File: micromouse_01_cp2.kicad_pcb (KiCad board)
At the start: 4 copper layers, 52 x 60 mm, 94 parts, among them IC1 MPU-6500, IC2 DRV8835DSSR, IC3 ADS7066IRTER, IC4 PCA9632TK,118, J2 Fan+, J3 Fan-, J4 Battery, J5 Battery, M1 MK06-4.5, M2 MK06-4.5, Q1 SiA910, Q5 SiA519, Q6 SiA519, Q7 SiA519, Q8 SiA519, Q9 SSM6J808R_LXHF, SW1 SSSS810701, U1 MA730, U10 LBR-127HLD, U11 LBR-127HLD, U12 ESP32-S3-MINI-1-N8, U2 MA730, U4 SMT-0440-S-R, U5 WS2812-2020, U7 LXDC55FAAA-203, U8 LBR-127HLD, U9 LBR-127HLD

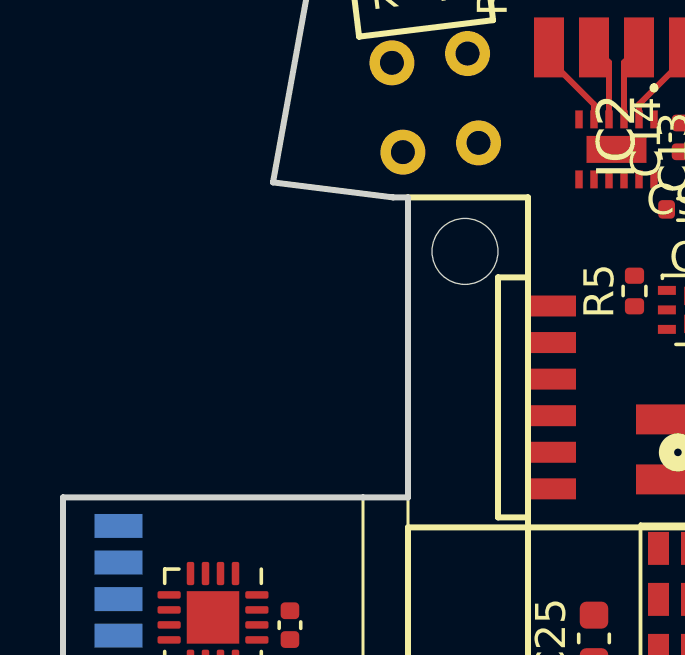
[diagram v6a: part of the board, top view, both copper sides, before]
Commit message: change encoder footprint
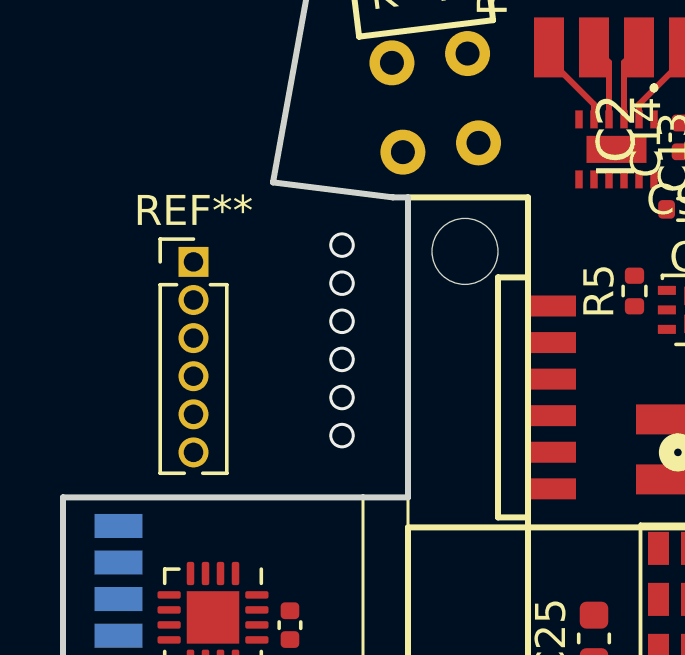
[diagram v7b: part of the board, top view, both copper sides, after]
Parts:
- added REF**: PinHeader_1x06_P1.27mm_Vertical, Connector_PinHeader_1.27mm:PinHeader_1x06_P1.27mm_Vertical, F.Cu at (129.3, 75.7)
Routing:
- net (no net): vias 0 -> 6
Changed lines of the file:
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@@
     )
   )
+  (footprint "Connector_PinHeader_1.27mm:PinHeader_1x06_P1.27mm_Vertical" (layer "F.Cu")
+    (at 129.35 75.65)
+    (descr "Through hole straight pin header, 1x06, 1.27mm pitch, single row")
+    (tags "Through hole pin header THT 1x06 1.27mm single row")
+    (attr through_hole)
+    (fp_text reference "REF**" (at 0 -1.695) (layer "F.SilkS")
+        (effects (font (size 1 1) (thickness 0.15)))
+    )
+    (fp_text value "PinHeader_1x06_P1.27mm_Vertical" (at 0 8.045) (layer "F.Fab")
+        (effects (font (size 1 1) (thickness 0.15)))
+    )
+    (fp_text user "${REFERENCE}" (at 0 3.175 90) (layer "F.Fab")
+        (effects (font (size 1 1) (thickness 0.15)))
+    )
+    (fp_line (start -1.11 -0.76) (end 0 -0.76)
+      (stroke (width 0.12) (type solid)) (layer "F.SilkS"))
+    (fp_line (start -1.11 0) (end -1.11 -0.76)
+      (stroke (width 0.12) (type solid)) (layer "F.SilkS"))
+    (fp_line (start -1.11 0.76) (end -1.11 7.045)
+      (stroke (width 0.12) (type solid)) (layer "F.SilkS"))
+    (fp_line (start -1.11 0.76) (end -0.563471 0.76)
+      (stroke (width 0.12) (type solid)) (layer "F.SilkS"))
+    (fp_line (start -1.11 7.045) (end -0.30753 7.045)
+      (stroke (width 0.12) (type solid)) (layer "F.SilkS"))
+    (fp_line (start 0.30753 7.045) (end 1.11 7.045)
+      (stroke (width 0.12) (type solid)) (layer "F.SilkS"))
+    (fp_line (start 0.563471 0.76) (end 1.11 0.76)
+      (stroke (width 0.12) (type solid)) (layer "F.SilkS"))
+    (fp_line (start 1.11 0.76) (end 1.11 7.045)
+      (stroke (width 0.12) (type solid)) (layer "F.SilkS"))
+    (fp_line (start -1.55 -1.15) (end -1.55 7.5)
+      (stroke (width 0.05) (type solid)) (layer "F.CrtYd"))
+    (fp_line (start -1.55 7.5) (end 1.55 7.5)
+      (stroke (width 0.05) (type solid)) (layer "F.CrtYd"))
+    (fp_line (start 1.55 -1.15) (end -1.55 -1.15)
+      (stroke (width 0.05) (type solid)) (layer "F.CrtYd"))
+    (fp_line (start 1.55 7.5) (end 1.55 -1.15)
+      (stroke (width 0.05) (type solid)) (layer "F.CrtYd"))
+    (fp_line (start -1.05 -0.11) (end -0.525 -0.635)
+      (stroke (width 0.1) (type solid)) (layer "F.Fab"))
+    (fp_line (start -1.05 6.985) (end -1.05 -0.11)
+      (stroke (width 0.1) (type solid)) (layer "F.Fab"))
+    (fp_line (start -0.525 -0.635) (end 1.05 -0.635)
+      (stroke (width 0.1) (type solid)) (layer "F.Fab"))
+    (fp_line (start 1.05 -0.635) (end 1.05 6.985)
+      (stroke (width 0.1) (type solid)) (layer "F.Fab"))
+    (fp_line (start 1.05 6.985) (end -1.05 6.985)
+      (stroke (width 0.1) (type solid)) (layer "F.Fab"))
+    (pad "1" thru_hole rect (at 0 0) (size 1 1) (drill 0.65) (layers "*.Cu" "*.Mask"))
+    (pad "2" thru_hole oval (at 0 1.27) (size 1 1) (drill 0.65) (layers "*.Cu" "*.Mask"))
+    (pad "3" thru_hole oval (at 0 2.54) (size 1 1) (drill 0.65) (layers "*.Cu" "*.Mask"))
+    (pad "4" thru_hole oval (at 0 3.81) (size 1 1) (drill 0.65) (layers "*.Cu" "*.Mask"))
+    (pad "5" thru_hole oval (at 0 5.08) (size 1 1) (drill 0.65) (layers "*.Cu" "*.Mask"))
+    (pad "6" thru_hole oval (at 0 6.35) (size 1 1) (drill 0.65) (layers "*.Cu" "*.Mask"))
+    (model "${KICAD6_3DMODEL_DIR}/Connector_PinHeader_1.27mm.3dshapes/PinHeader_1x06_P1.27mm_Vertical.wrl"
+      (offset (xyz 0 0 0))
+      (scale (xyz 1 1 1))
+      (rotate (xyz 0 0 0))
+    )
+  )
   (footprint "Package_TO_SOT_SMD:Vishay_PowerPAK_SC70-6L_Dual" (layer "F.Cu")
     (at 149.7 92.7 -90)
@@
     (effects (font (size 1 1) (thickness 0.2) bold) (justify bottom mirror))
   )
+  (via (at 134.3 76.36) (size 0.85) (drill 0.65) (layers "F.Cu" "B.Cu") (net 0))
+  (via (at 134.3 77.63) (size 0.85) (drill 0.65) (layers "F.Cu" "B.Cu") (net 0))
+  (via (at 134.3 80.17) (size 0.85) (drill 0.65) (layers "F.Cu" "B.Cu") (net 0))
+  (via (at 134.3 81.44) (size 0.85) (drill 0.65) (layers "F.Cu" "B.Cu") (net 0))
+  (via (at 134.3 78.9) (size 0.85) (drill 0.65) (layers "F.Cu" "B.Cu") (net 0))
+  (via (at 134.3 75.09) (size 0.85) (drill 0.65) (layers "F.Cu" "B.Cu") (net 0))
   (segment (start 165.4375 108) (end 165.4375 106.8425) (width 0.2) (layer "F.Cu") (net 1))
   (segment (start 158 108.25) (end 159.5 108.25) (width 0.3) (layer "F.Cu") (net 1))

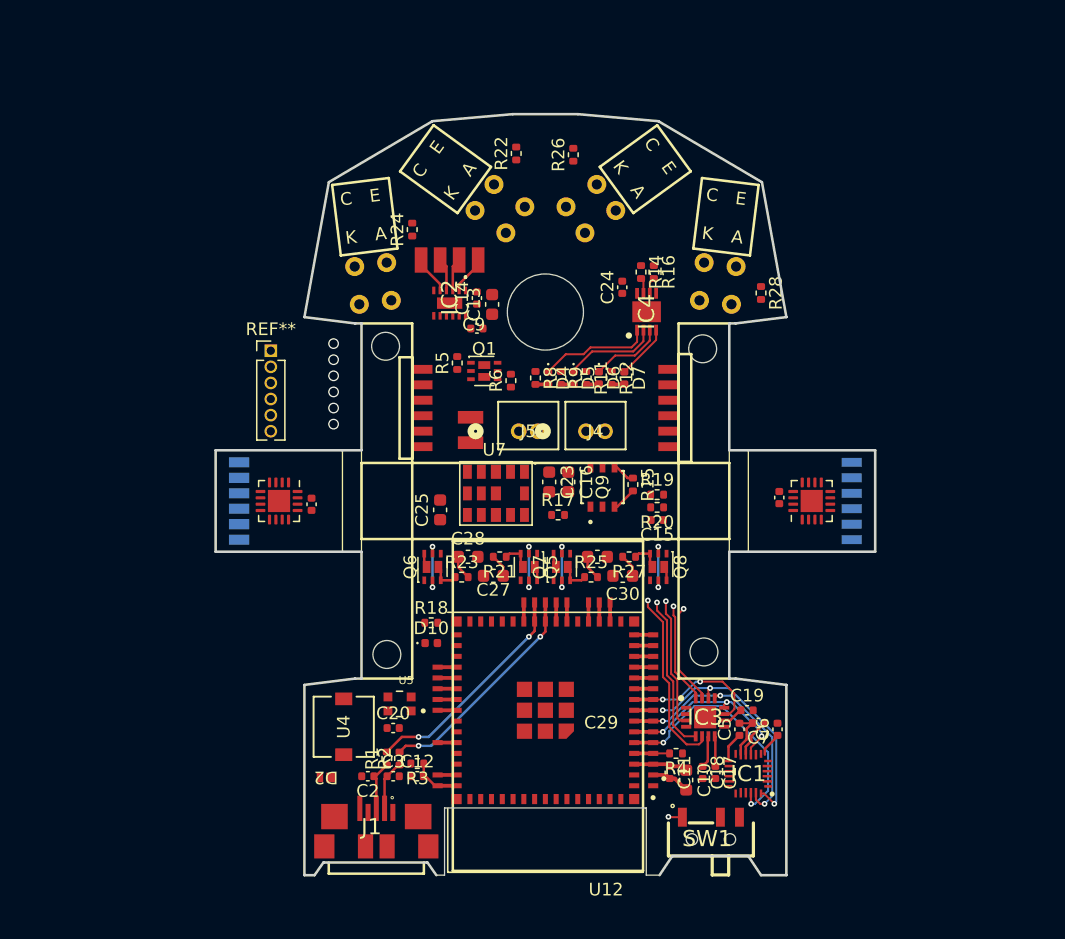
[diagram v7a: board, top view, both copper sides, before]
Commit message: Added 3D model
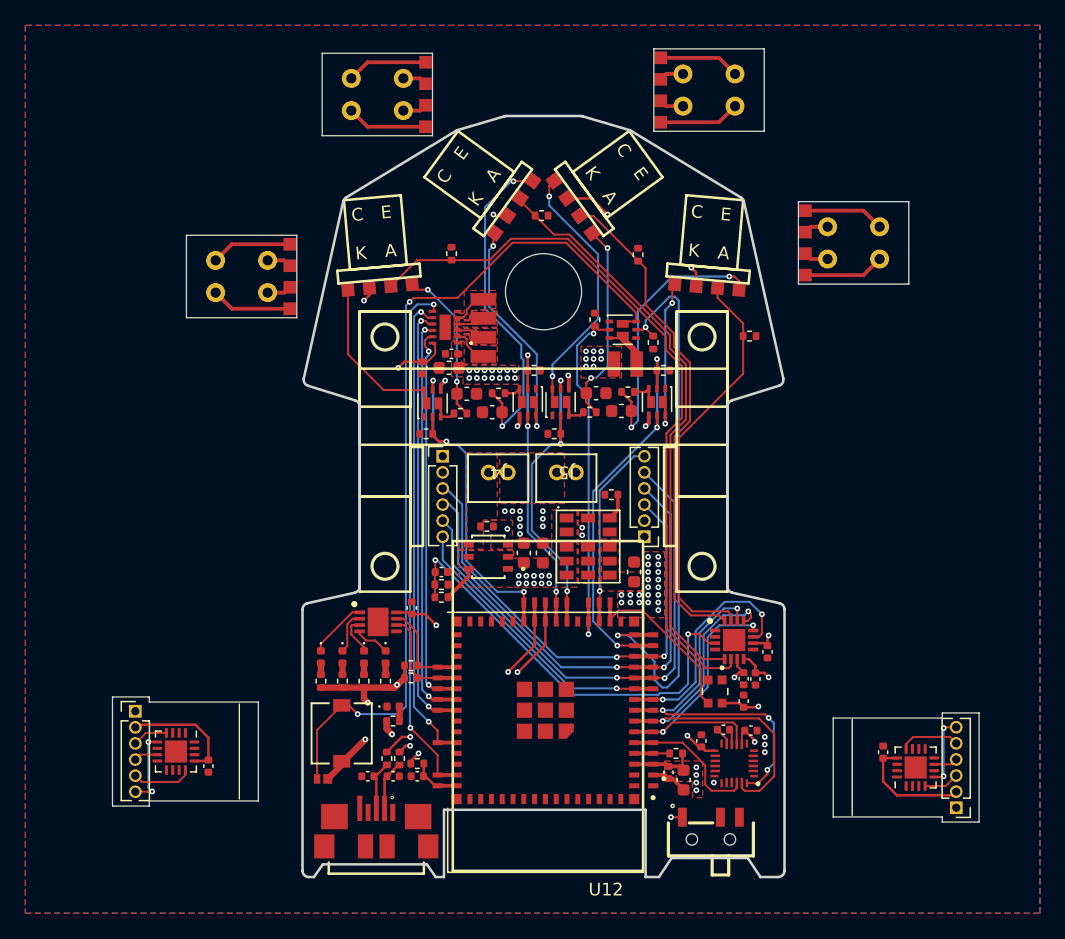
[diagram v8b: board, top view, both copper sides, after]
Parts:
- removed the REF** at (141.3, 80.2)
- removed the REF** at (160.7, 80.2)
- removed the REF** at (126.8, 87.5)
- removed the REF** at (175.2, 87.5)
- added R10: 47k, Resistor_SMD:R_0402_1005Metric, F.Cu at (141.6, 82.2)
- added R13: 47k, Resistor_SMD:R_0402_1005Metric, F.Cu at (151.7, 82.2)
- added R29: 47k, Resistor_SMD:R_0402_1005Metric, F.Cu at (160.3, 77.2)
- added R7: 47k, Resistor_SMD:R_0402_1005Metric, F.Cu at (150.1, 77.2)
- added REF**: LBR-127HLD_PAD, footprints:LBR-127HLD_PAD, F.Cu at (160.1, 55.1)
- added REF**: PinHeader_1x06_P1.27mm_Vertical, Connector_PinHeader_1.27mm:PinHeader_1x06_P1.27mm_Vertical, F.Cu at (183.4, 111.7)
- added REF**: LBR-127HLD_PAD, footprints:LBR-127HLD_PAD, F.Cu at (171.5, 67.2)
- added REF**: LBR-127HLD_THT, footprints:LBR-127HLD_THT, F.Cu at (125.0, 69.8)
- added REF**: LBR-127HLD_PAD, footprints:LBR-127HLD_PAD, F.Cu at (130.8, 69.8)
- added REF**: LBR-127HLD_THT, footprints:LBR-127HLD_THT, F.Cu at (135.7, 55.5)
- added REF**: LBR-127HLD_THT, footprints:LBR-127HLD_THT, F.Cu at (177.3, 67.2)
- added REF**: PinHeader_1x06_P1.27mm_Vertical, Connector_PinHeader_1.27mm:PinHeader_1x06_P1.27mm_Vertical, F.Cu at (158.8, 90.3)
- added REF**: LBR-127HLD_PAD, footprints:LBR-127HLD_PAD, F.Cu at (141.6, 55.5)
- added REF**: LBR-127HLD_PAD, footprints:LBR-127HLD_PAD, F.Cu at (148.5, 64.3)
- added REF**: LBR-127HLD_PAD, footprints:LBR-127HLD_PAD, F.Cu at (153.2, 64.3)
- added REF**: PinHeader_1x06_P1.27mm_Vertical, Connector_PinHeader_1.27mm:PinHeader_1x06_P1.27mm_Vertical, F.Cu at (118.7, 104.1)
- added REF**: LBR-127HLD_PAD, footprints:LBR-127HLD_PAD, F.Cu at (138.0, 70.7)
- added REF**: LBR-127HLD_PAD, footprints:LBR-127HLD_PAD, F.Cu at (163.7, 70.7)
- added REF**: LBR-127HLD_THT, footprints:LBR-127HLD_THT, F.Cu at (165.9, 55.1)
- moved U2 54.4 mm to (180.2, 108.5), turned to 90 degrees
- moved U1 53.9 mm to (121.9, 107.2), turned to -90 degrees
- moved C4 49.7 mm to (124.4, 108.4)
- moved C8 49.1 mm to (177.6, 107.3)
- moved R16 37.3 mm to (140.4, 101.5), turned to 0 degrees
- moved R14 35.9 mm to (140.4, 100.5), turned to 0 degrees
- moved IC4 32.3 mm to (137.8, 97.0), turned to 0 degrees
- moved C24 30.2 mm to (140.5, 95.9)
- moved R12 29.8 mm to (138.4, 101.7), turned to 90 degrees
- moved R11 29.6 mm to (136.7, 101.7), turned to 90 degrees
- moved R9 29.5 mm to (135.0, 101.7), turned to 90 degrees
- moved R8 29.3 mm to (133.3, 101.7), turned to 90 degrees
- moved D7 28.9 mm to (138.4, 99.8)
- moved D6 28.8 mm to (136.7, 99.8)
- moved D5 28.6 mm to (135.0, 99.8)
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- renumbered REF** to REF*
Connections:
- IC3 pad 5: SENS_FL -> SENS_L
- IC3 pad 6: SENS_L -> SENS_FL
- REF** pad 1: (no net) -> GND
- REF** pad 2: (no net) -> +3V3
- REF** pad 3: (no net) -> ENC_MOSI
- REF** pad 4: (no net) -> ENC_MISO
- REF** pad 5: (no net) -> ENC_CLK
- REF** pad 6: (no net) -> ENCL_CS
- U12 pad 14: LED_L -> LED_FR
- U12 pad 17: BUZZER -> NeoPixel
- U12 pad 19: NeoPixel -> BUZZER
- U12 pad 21: LED_FL -> LED_R
- U12 pad 22: LED_R -> LED_L
- U12 pad 25: LED_FR -> LED_FL
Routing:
- net +3V3: track 15.2 -> 282.9 mm, vias 0 -> 46
- net Net-(D2-A): track 0.00 -> 68.1 mm, vias 0 -> 2
- net ENC_CLK: track 1.50 -> 51.4 mm, vias 0 -> 2
- net SENS_FL: track 12.3 -> 59.4 mm, vias 1 -> 0
- net FAN_PWM: track 1.50 -> 46.2 mm, vias 0 -> 2
- net ENC_MISO: track 1.50 -> 44.1 mm, vias 0 -> 2
- net ENC_MOSI: track 1.50 -> 44.0 mm, vias 0 -> 2
- net MOT2_ENBL: track 1.50 -> 41.6 mm, vias 0 -> 2
- net MOT2_PHASE: track 1.50 -> 37.7 mm, vias 0 -> 2
- net MOT1_ENBL: track 1.50 -> 35.7 mm, vias 0 -> 2
- net SENS_R: track 7.97 -> 41.6 mm, vias 1 -> 0
- net SENS_L: track 14.3 -> 47.6 mm, vias 1 -> 0
- net +BATT: track 0.00 -> 32.1 mm, vias 0 -> 32
- net MOT1_PHASE: track 1.50 -> 33.6 mm, vias 0 -> 2
- net Net-(C27-Pad1): track 1.83 -> 33.1 mm, vias 0 -> 2
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- added copper zone on F.Cu, net +3V3
- added copper zone on In1.Cu, net +3V3
- added copper zone on F.Cu, net +BATT
- added copper zone on In1.Cu, net +BATT
- added copper zone on B.Cu, net GND
- added copper zone on F.Cu, net GND
- added copper zone on In1.Cu, net GND
- added copper zone on In2.Cu, net GND
- added copper zone on F.Cu, net Net-(IC2-AOUT1)
- added copper zone on F.Cu, net Net-(IC2-AOUT2)
- added copper zone on F.Cu, net Net-(IC2-BOUT1)
- added copper zone on F.Cu, net Net-(IC2-BOUT2)
- added copper zone on F.Cu, net Net-(J4-Pin_1)
- added copper zone on F.Cu, net Net-(J4-Pin_2)
- added copper zone on F.Cu, net Net-(Q9-G)
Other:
- board size 52 x 60 mm -> 68.3 x 65.3 mm
- board text added: "reRoMouse v2.0 2024 Spt Designed by Yujiro & Saposen"
- board text removed: "reRoMouse v1.1 2024 Apr Designed by Yujiro & Saposen"
